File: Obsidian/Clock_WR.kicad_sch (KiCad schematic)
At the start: 74 parts, among them U12 LP5951MF-3.0/NOPB, U13 LM336M-2.5, U14 DAC8551IADGKR, U15 DAC8551IADGKR, U16 CDCM61002RHBR, U3 Si5351A-B-GT, Y1 9132S-Y25.000N33DT1J, Y2 VM53S3-25.000-2.5/-30+75, Y3 OSC_20MHZ_IQD_LFVCXO026156, Y6 ABM8W-25.0000MHZ-8-D1X-T3

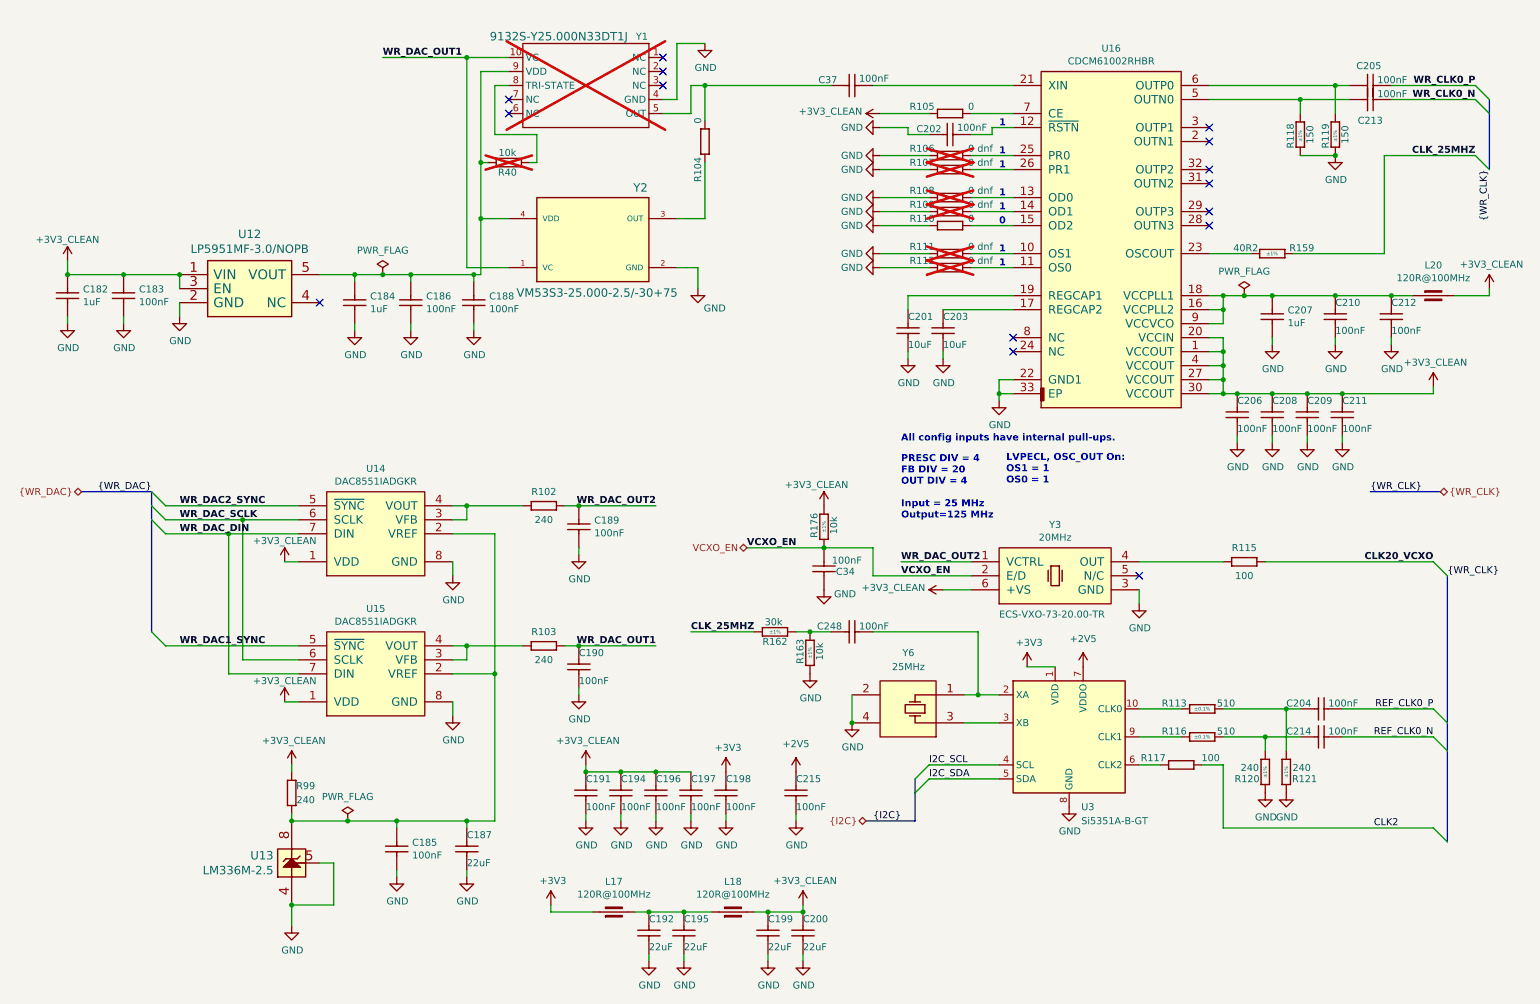
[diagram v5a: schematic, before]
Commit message: Adding documentation for configuration with flash memory, adding more comments to schematic
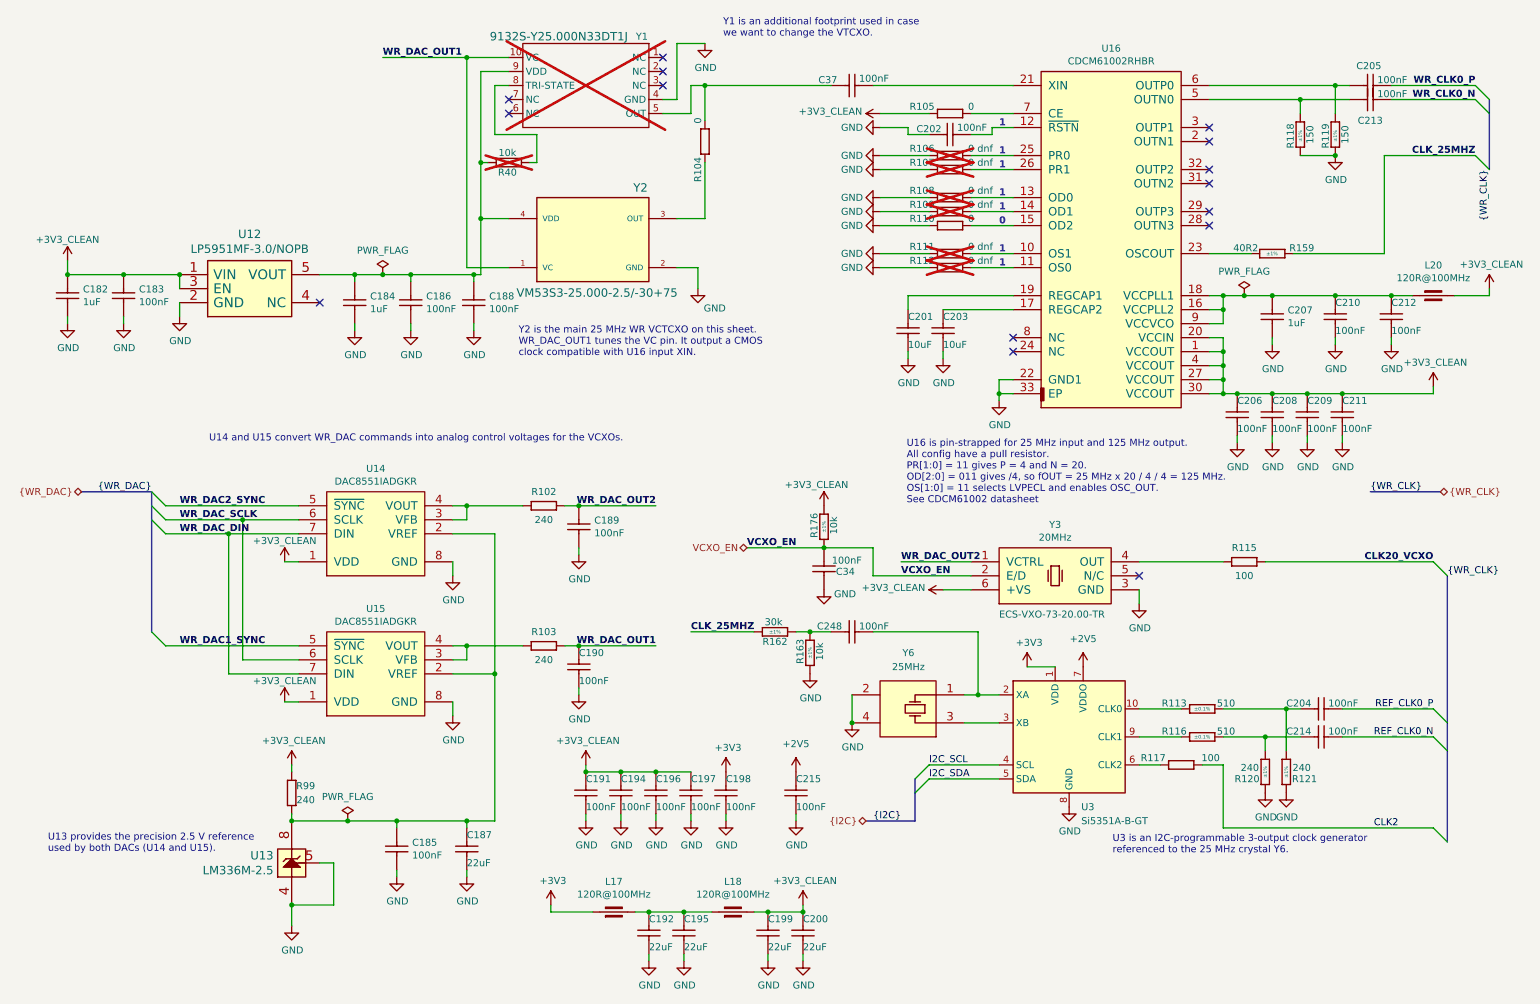
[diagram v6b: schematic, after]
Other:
- note added: "U13 provides the precision 2.5 V reference used by both DACs (U14 and U15)."
- note added: "U14 and U15 convert WR_DAC commands into analog control voltages for the VCXOs."
- note added: "U16 is pin-strapped for 25 MHz input and 125 MHz output. All config have a pull resistor. PR[1:0] = 11 gives P = 4 and N = 20. OD[2:0] = 011 gives /4, so fOUT = 25 MHz x 20 / 4 / 4 = 125 MHz. OS[1:0] = 11 selects LVPECL and enables OSC_OUT. See CDCM61002 datasheet"
- note added: "U3 is an I2C-programmable 3-output clock generator referenced to the 25 MHz crystal Y6."
- note added: "Y1 is an additional footprint used in case we want to change the VTCXO."
- note added: "Y2 is the main 25 MHz WR VCTCXO on this sheet. WR_DAC_OUT1 tunes the VC pin. It output a CMOS clock compatible with U16 input XIN."
- note removed: "All config inputs have internal pull-ups."
- note removed: "LVPECL, OSC_OUT On: OS1 = 1 OS0 = 1"
- note removed: "PRESC DIV = 4 FB DIV = 20 OUT DIV = 4 Input = 25 MHz Output=125 MHz"
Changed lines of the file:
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@@
+		)
+	)
+	(text "Y2 is the main 25 MHz WR VCTCXO on this sheet.\nWR_DAC_OUT1 tunes the VC pin. It output a CMOS\nclock compatible with U16 input XIN. "
+		(exclude_from_sim no)
+		(at 102.108 71.882 0)
+		(effects
+			(font
+				(size 1.27 1.27)
+			)
+			(justify left)
 		)
 	)
@@
 		)
 	)
-	(text "PRESC DIV = 4\nFB DIV = 20\nOUT DIV = 4\n\nInput = 25 MHz\nOutput=125 MHz"
+	(text "U16 is pin-strapped for 25 MHz input and 125 MHz output.\nAll config have a pull resistor.\nPR[1:0] = 11 gives P = 4 and N = 20.\nOD[2:0] = 011 gives /4, so fOUT = 25 MHz x 20 / 4 / 4 = 125 MHz.\nOS[1:0] = 11 selects LVPECL and enables OSC_OUT.\nSee CDCM61002 datasheet"
 		(exclude_from_sim no)
-		(at 171.45 104.14 0)
+		(at 172.466 95.504 0)
 		(effects
 			(font
 				(size 1.27 1.27)
-				(thickness 0.254)
-				(bold yes)
 			)
-			(justify left bottom)
+			(justify left)
 		)
 	)
@@
 		)
 	)
-	(text "LVPECL, OSC_OUT On:\nOS1 = 1\nOS0 = 1"
+	(text "U14 and U15 convert WR_DAC commands into analog control voltages for the VCXOs."
 		(exclude_from_sim no)
-		(at 190.5 97.79 0)
+		(at 45.974 89.408 0)
 		(effects
 			(font
 				(size 1.27 1.27)
-				(thickness 0.254)
-				(bold yes)
 			)
-			(justify left bottom)
+			(justify left)
 		)
 	)
-	(text "All config inputs have internal pull-ups."
+	(text "U13 provides the precision 2.5 V reference \nused by both DACs (U14 and U15)."
 		(exclude_from_sim no)
-		(at 171.45 90.17 0)
+		(at 16.764 162.814 0)
 		(effects
 			(font
 				(size 1.27 1.27)
-				(thickness 0.254)
-				(bold yes)
 			)
-			(justify left bottom)
+			(justify left)
 		)
 	)
+	(text "Y1 is an additional footprint used in case \nwe want to change the VTCXO."
+		(exclude_from_sim no)
+		(at 139.192 14.986 0)
+		(effects
+			(font
+				(size 1.27 1.27)
+			)
+			(justify left)
+		)
+	)
+	(text "U3 is an I2C-programmable 3-output clock generator \nreferenced to the 25 MHz crystal Y6."
+		(exclude_from_sim no)
+		(at 209.804 163.068 0)
+		(effects
+			(font
+				(size 1.27 1.27)
+			)
+			(justify left)
+		)
+	)

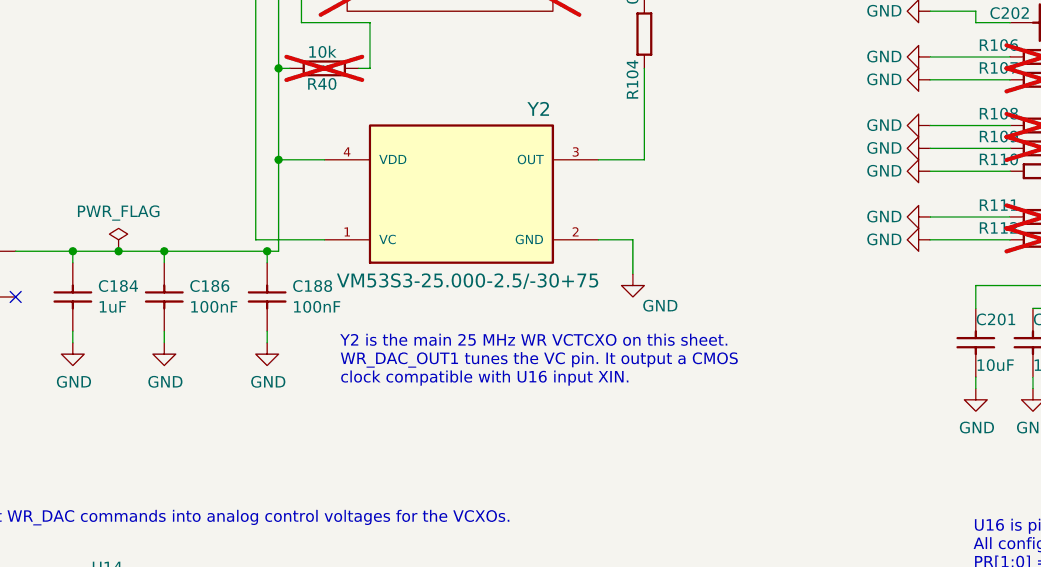
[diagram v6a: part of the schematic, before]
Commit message: adding comments, and test point for U12 (power supply in clock sheet)
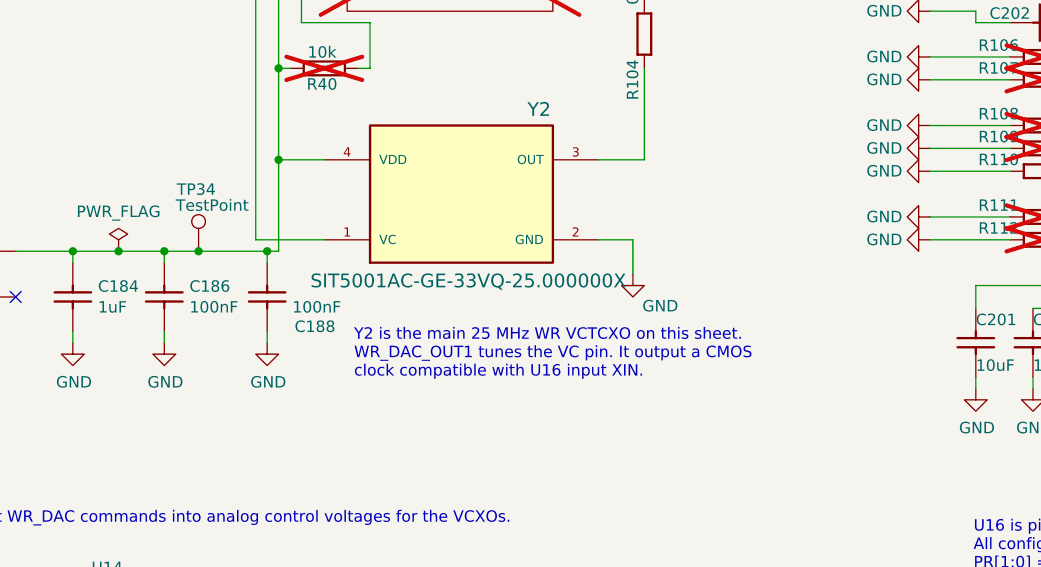
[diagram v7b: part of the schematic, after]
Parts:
- added TP34: TestPoint, TestPoint:TestPoint_Pad_D1.5mm, symbol Library_Symbol:TestPoint
- Y2: value VM53S3-25.000-2.5/-30+75 -> SIT5001AC-GE-33VQ-25.000000X
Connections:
- net at C184.1, C186.1, C188.1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: now also TP34.1

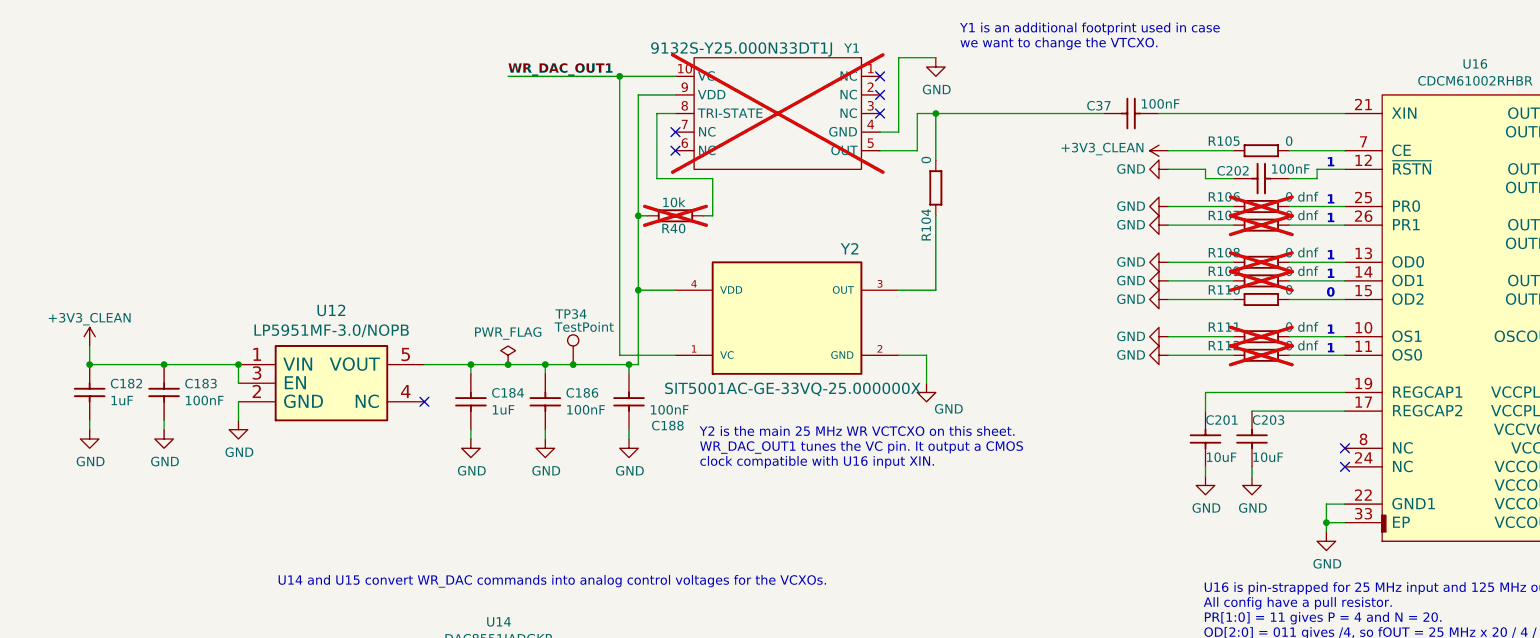
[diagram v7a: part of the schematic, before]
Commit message: adding LVCMOS conversiont circuit
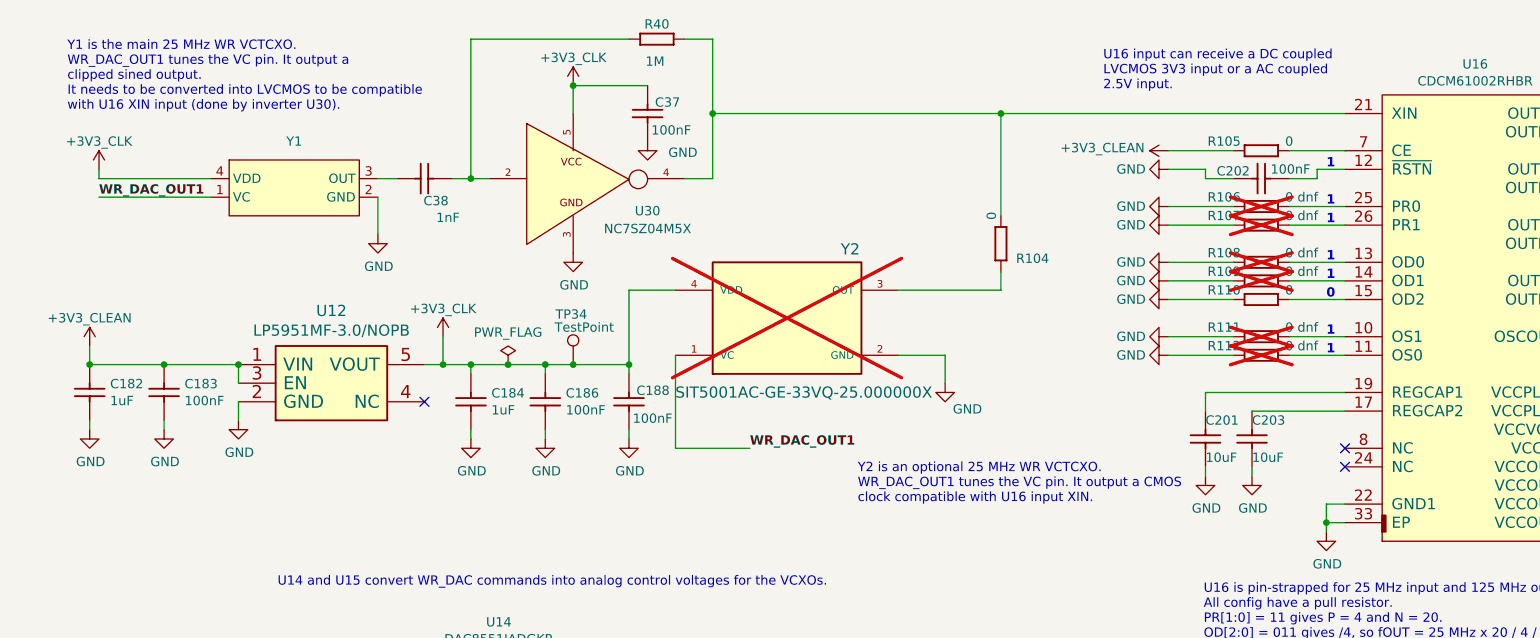
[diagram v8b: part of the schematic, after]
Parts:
- removed C37: CC0402_100NF_50V_10%_X7R, Footprint:CAPC1005X55N, symbol Library_Symbol:CC0402_100NF_50V_10%_X7R
- removed R40: R0402_10K_1%_0.0625W_100PPM, Footprint:RESC1005X40N, symbol Library_Symbol:R0402_10K_1%_0.0625W_100PPM
- removed Y1: 9132S-Y25.000N33DT1J, ProLib_pcs_2026-03-30:OSC-SMD_10P-L7.0-W5.0-BL_OHXXXXXXX, symbol Library_Symbol:9875HA-25.000N33FT1JL
- added C37: CC0201_100NF_6.3V_10%_X5R, Footprint:CAPC0603X33N, symbol Library_Symbol:CC0201_100NF_6.3V_10%_X5R
- added C38: CC0201_1NF_25V_5%_C0G, Footprint:CAPC0603X33N, symbol Library_Symbol:CC0201_100NF_6.3V_10%_X5R
- added R40: R0402_1MR_1%_0.0625W_100PPM, Footprint:RESC1005X40N, symbol Library_Symbol:R0402_240R_1%_0.0625W_100PPM
- added U30: NC7SZ04M5X, Footprint:SOT95P280X145-5N, symbol Library_Symbol:NC7SZ04M5X
- added Y1: 25MHz, Footprint:CRYSTAL-SMD_4P-L3.2-W2.5-BL-1_9132S-Y25.000N33DT1J, symbol Library_Symbol:9132S-Y25.000N33DT1J
- Y2: now not fitted; now left out of the parts list
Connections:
- net GND: now also C37.2, U30.3, Y1.2 (GND)
- net WR_DAC_OUT1: now also Y1.1 (VC)
- net +3V3_CLK: now reaches C184.1, C186.1, C188.1, TP34.1, U12.5 (VOUT), Y2.4 (VDD)
- net +3V3_CLK: now also C37.1, U30.5, Y1.4 (VDD)
- net at R104.2: now also U16.21 (XIN), R40.1, U30.4
- new net: C38.1, R40.2, U30.2
- new net: C38.2, Y1.3 (OUT)
- no-connect marks 15 -> 10
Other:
- note added: "U16 input can receive a DC coupled LVCMOS 3V3 input or a AC coupled 2.5V input."
- note added: "Y1 is the main 25 MHz WR VCTCXO. WR_DAC_OUT1 tunes the VC pin. It output a clipped sined output. It needs to be converted into LVCMOS to be compatible with U16 XIN input (done by inverter U30)."
- note added: "Y2 is an optional 25 MHz WR VCTCXO. WR_DAC_OUT1 tunes the VC pin. It output a CMOS clock compatible with U16 input XIN."
- note removed: "Y1 is an additional footprint used in case we want to change the VTCXO."
- note removed: "Y2 is the main 25 MHz WR VCTCXO on this sheet. WR_DAC_OUT1 tunes the VC pin. It output a CMOS clock compatible with U16 input XIN."
- moved on the sheet: R104
